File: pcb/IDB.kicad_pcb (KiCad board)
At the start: 2 copper layers, 77.2 x 50.8 mm, 38 parts, among them J1 Conn_01x10_Socket, J10 Conn_01x03_Socket, J11 Conn_01x03_Socket, J12 Conn_01x03_Socket, J13 Conn_01x03_Socket, J14 Conn_01x03_Socket, J15 Conn_01x03_Socket, J16 Conn_01x03_Socket, J17 Conn_01x03_Socket, J18 Conn_01x03_Socket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

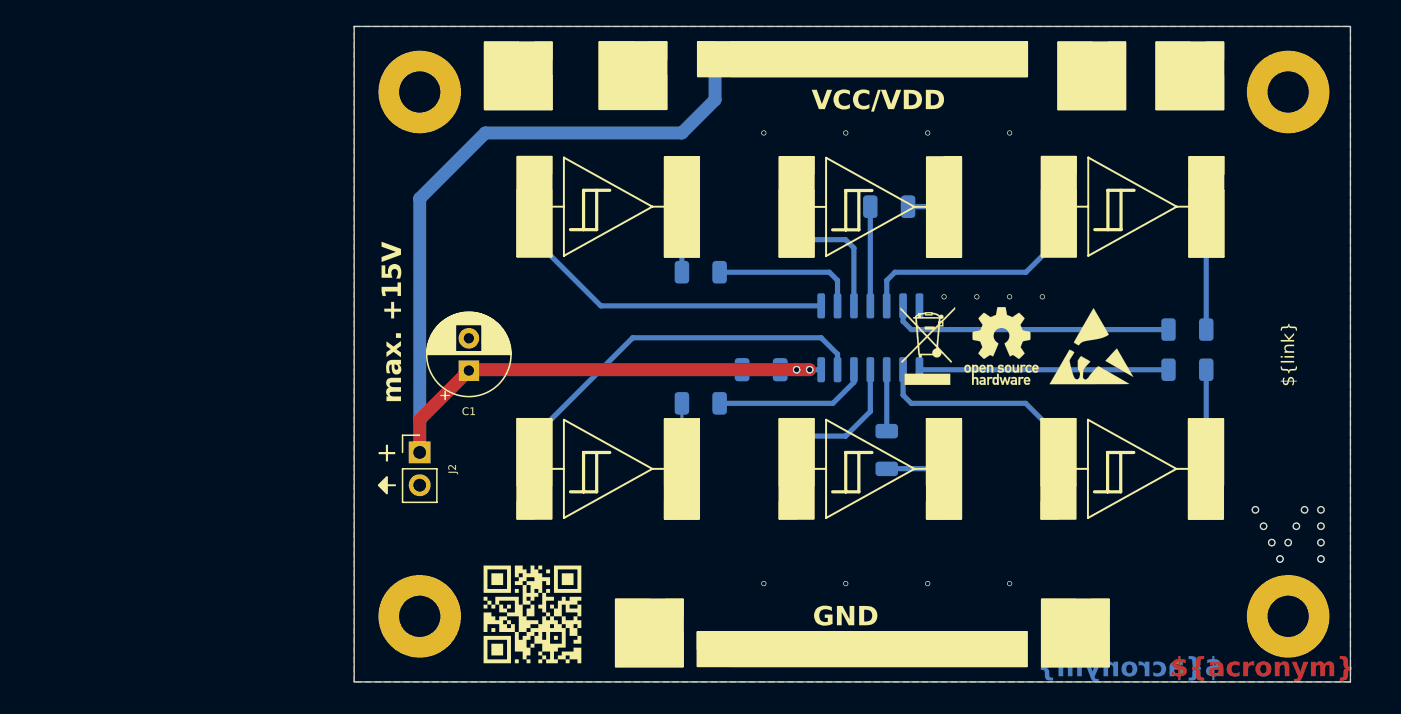
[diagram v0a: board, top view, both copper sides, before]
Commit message: Adapt edge cuts and dimensioning
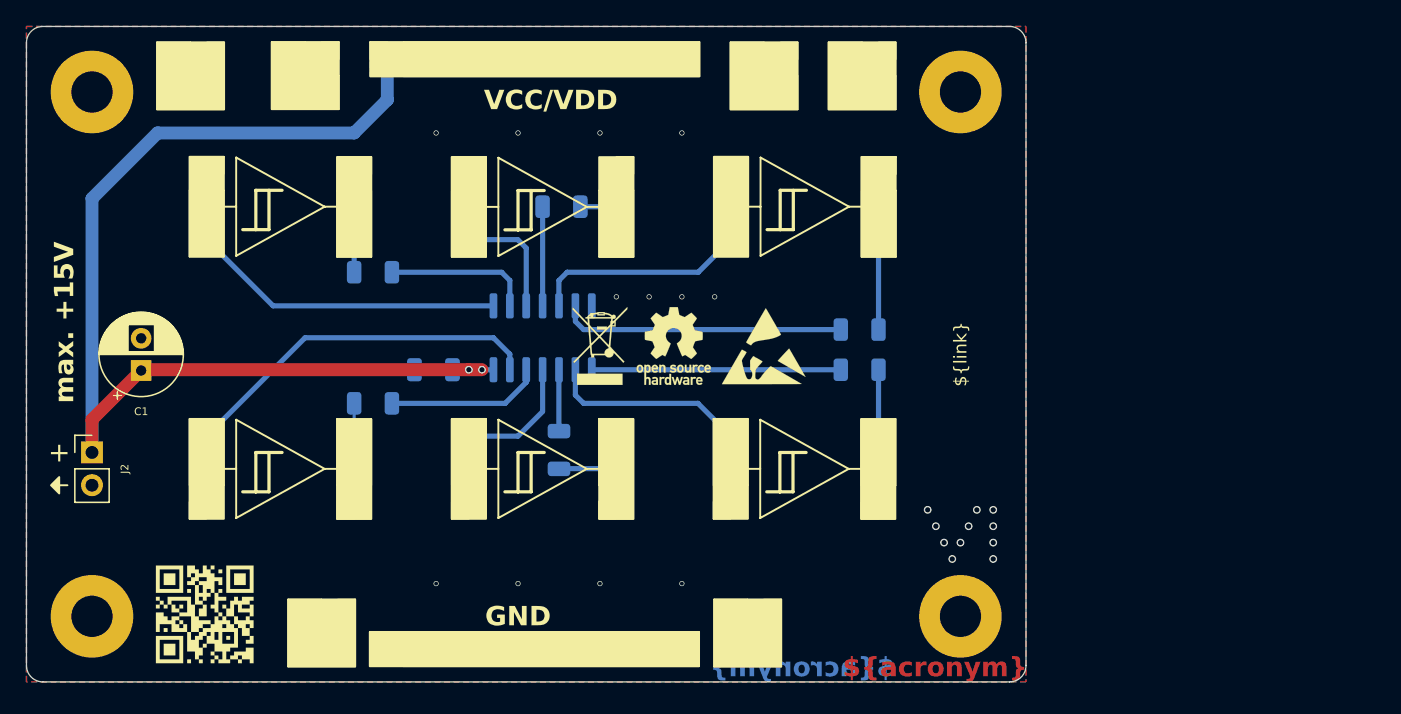
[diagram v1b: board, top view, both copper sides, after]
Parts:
- moved H1 25.4 mm to (124.5, 81.3)
- moved H2 25.4 mm to (124.5, 121.9)
- moved J2 25.4 mm to (124.5, 109.2)
- moved FID1 25.4 mm to (176.5, 101.0)
- moved FID3 25.4 mm to (169.5, 101.0)
- moved FID4 25.4 mm to (133.3, 121.9)
- moved J1 25.4 mm to (147.3, 78.7)
- moved J10 25.4 mm to (133.3, 113.0)
- moved J11 25.4 mm to (153.7, 113.0)
- moved J12 25.4 mm to (174.0, 113.0)
- moved J14 25.4 mm to (153.7, 87.6)
- moved J15 25.4 mm to (133.3, 87.6)
- moved J16 25.4 mm to (144.8, 113.0)
- moved J17 25.4 mm to (165.1, 113.0)
- moved J18 25.4 mm to (185.4, 113.0)
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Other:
- board size 77.2 x 50.8 mm -> 77.5 x 50.8 mm

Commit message: Add reverse polarity protection
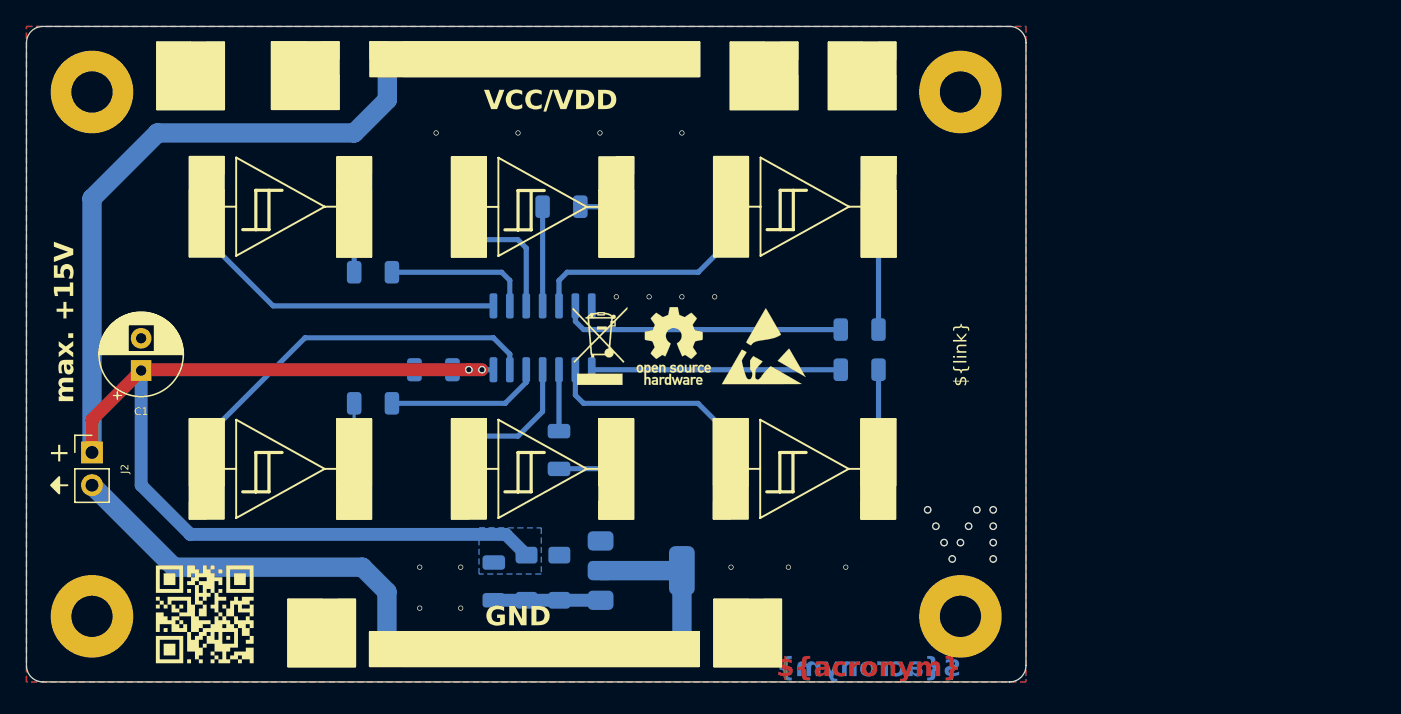
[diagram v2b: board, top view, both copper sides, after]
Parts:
- added D1: BAT43, Diode_SMD:D_MiniMELF, B.Cu at (158.1, 118.9)
- added D2: BZ5V1, Diode_SMD:D_MiniMELF, B.Cu at (160.7, 118.9)
- added Q1: BUK7880-55A, Package_TO_SOT_SMD:SOT-223-3_TabPin2, B.Cu at (167.0, 118.4)
- added R7: 1k, Resistor_SMD:R_1206_3216Metric, B.Cu at (155.6, 119.2)
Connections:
- J2 pad 2: GND -> Net-(J2-Pin_2)
- J3 pad 1: GND -> Net-(J2-Pin_2)
- J3 pad 10: GND -> Net-(J2-Pin_2)
- J3 pad 2: GND -> Net-(J2-Pin_2)
- J3 pad 3: GND -> Net-(J2-Pin_2)
- J3 pad 4: GND -> Net-(J2-Pin_2)
- J3 pad 5: GND -> Net-(J2-Pin_2)
- J3 pad 6: GND -> Net-(J2-Pin_2)
- J3 pad 7: GND -> Net-(J2-Pin_2)
- J3 pad 8: GND -> Net-(J2-Pin_2)
- J3 pad 9: GND -> Net-(J2-Pin_2)
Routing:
- net Net-(J2-Pin_2): track 0.00 -> 43.1 mm
- net VCC: track 86.4 -> 127.4 mm
- net Net-(D1-A): track 0.00 -> 8.28 mm
- net GND: vias 23 -> 26
- added copper zone on B.Cu, net Net-(J2-Pin_2)
